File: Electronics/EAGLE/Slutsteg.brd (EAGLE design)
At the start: 100 x 160 mm, 111 parts, among them CN2 OSTYK33102030-2, CN3 OSTYK33102030-2, IC1 MC78M12CDTG, IC10 TM8211, IC11 LM358LVIDR, IC3 TPA3251D2DDVR, IC4 TPA3244DDWR, IC8 ESP32-WROVER-IE-4MB, IC9 ZLDO1117G33TA, J2 0532610671

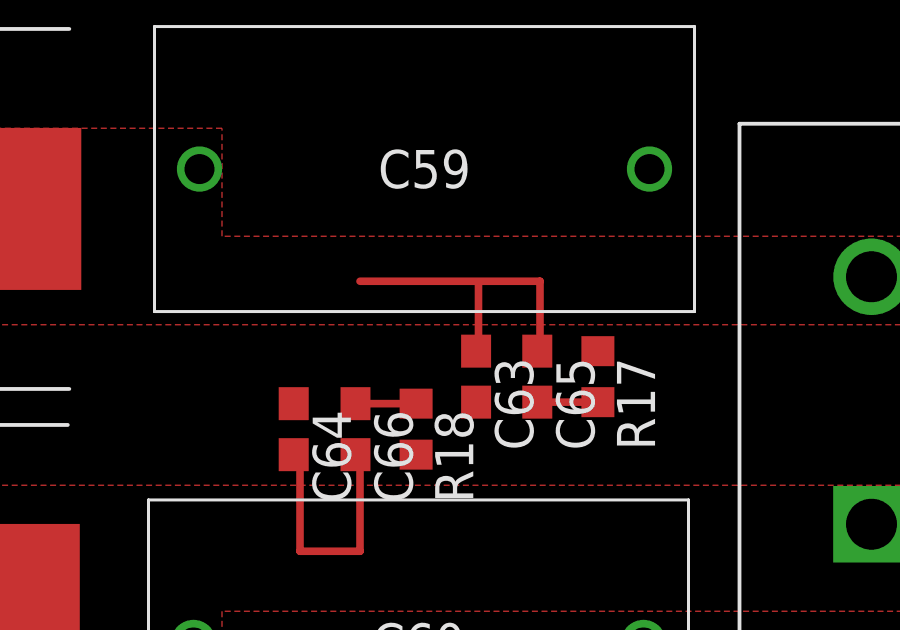
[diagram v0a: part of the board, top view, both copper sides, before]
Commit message: Added speaker connector models.
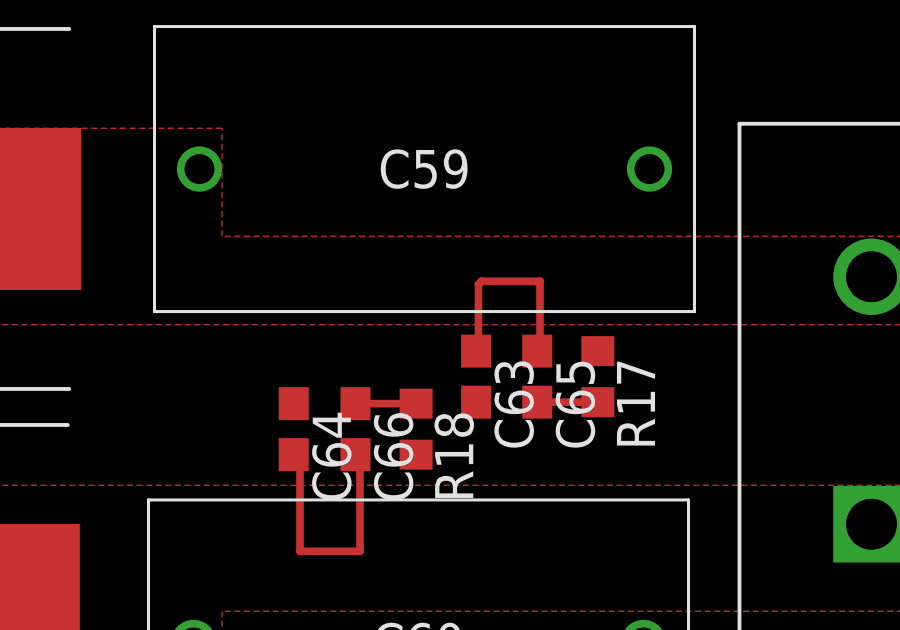
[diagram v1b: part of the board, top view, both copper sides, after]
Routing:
- net SPEAKER_L_0: track 10.6 -> 6.72 mm
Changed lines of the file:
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@@
 <drawing>
 <settings>
-<setting alwaysvectorfont="yes"/>
+<setting alwaysvectorfont="no"/>
 <setting verticaltext="up"/>
 </settings>
@@
 <attribute name="VALUE" x="-35.18" y="73.76" size="1.27" layer="27"/>
 </element>
-<element name="CN2" library="OSTYK33108030" package="OSTYK33108030-2" value="OSTYK33102030-2" x="88.05" y="101.9" smashed="yes" rot="R90">
+<element name="CN2" library="OSTYK33108030" package="OSTYK33108030-2" override_package3d_urn="urn:adsk.eagle:package:27162182/2" override_package_urn="urn:adsk.eagle:footprint:27162183/1" value="OSTYK33102030-2" x="88.05" y="101.9" smashed="yes" rot="R90">
 <attribute name="NAME" x="96.05" y="102.77" size="1.27" layer="25" rot="R90"/>
 </element>
-<element name="CN3" library="OSTYK33108030" package="OSTYK33108030-2" value="OSTYK33102030-2" x="88.05" y="75.8" smashed="yes" rot="R90">
+<element name="CN3" library="OSTYK33108030" package="OSTYK33108030-2" override_package3d_urn="urn:adsk.eagle:package:27162207/2" override_package_urn="urn:adsk.eagle:footprint:27162209/1" value="OSTYK33102030-2" x="88.05" y="75.8" smashed="yes" rot="R90">
 <attribute name="NAME" x="96.05" y="76.67" size="1.27" layer="25" rot="R90"/>
 </element>
@@
 </polygon>
 <wire x1="77" y1="107.76" x2="76.91" y2="107.67" width="0.1524" layer="1"/>
-<wire x1="74.95" y1="109.9" x2="74.95" y2="107.75" width="0.254" layer="1"/>
+<wire x1="74.95" y1="107.75" x2="74.95" y2="109.9" width="0.254" layer="1"/>
 <wire x1="74.87" y1="107.67" x2="74.95" y2="107.75" width="0.254" layer="1"/>
-<wire x1="71" y1="110" x2="77" y2="110" width="0.254" layer="1"/>
 <wire x1="77" y1="110" x2="77" y2="107.76" width="0.254" layer="1"/>
+<wire x1="74.95" y1="109.9" x2="75.05" y2="110" width="0.254" layer="1"/>
+<wire x1="75.05" y1="110" x2="77" y2="110" width="0.254" layer="1"/>
 </signal>
 <signal name="I/O-0">

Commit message: Sammanfogat design blocks
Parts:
- added C12: 150nF/25V, rcl:C0603
- added C13, C14, C55: 1uF/25V, rcl:C0603
- added C56: 33nF/25V, rcl:C0603
- added C87, C88, C89, C90, C91, C92: 100nF/25V, rcl:C0603
- added IC6, IC7: LM324D, SamacSys_Parts:SOIC127P600X175-14N
- added R39, R40, R41, R42, R43, R44: 100K/5%/0.1W, rcl:R0603
- added R45, R46: 1K/5%/0.1W, rcl:R0603
- added R47, R48: 18K/5%/0.1W, rcl:R0603
- added R49, R50, R51, R52, R53, R54, R55: 10K/5%/0.1W, rcl:R0603
- added SW3, SW4: PDB181-K420F-103A2, PDB181-K420F-103A2:SW_420F-103A2_BRN
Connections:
- new net 6V_BUFFER: IC6.1, IC6.2, IC6.5, IC7.12, IC7.3, R51.2, R54.2
- new net BASE_OUT: C56.1, R48.1
- new net BASE_VOLUME: IC6.7
- new net LEFT: C87.1, IC6.13, IC6.14, R45.2
- new net LEFT_OUT: IC7.1, SW3.2, SW3.3
- new net LEFT_VOLUME: IC7.6, IC7.7, R50.1, R52.2
- new net N$46: C13.2, IC6.12, R39.1, R40.2
- new net N$47: C14.2, IC6.10, R41.2, R42.1
- new net N$50: C55.1, IC6.3, R43.1, R44.2
- new net N$66: R45.1, R46.1, R47.2
- new net N$67: C12.2, R47.1, R48.2, R49.2
- new net N$68: C56.2, IC6.6, R49.1
- new net N$69: C87.2, C88.1, R50.2
- new net N$70: C88.2, IC7.5, R51.1
- new net N$71: IC7.2, R52.1, SW3.1
- new net N$72: C90.1, IC7.10, R54.1
- new net N$73: C89.1, C90.2, R53.2
- new net N$74: IC7.13, R55.2, SW4.1
- new net RIGHT: C89.2, IC6.8, IC6.9, R46.2
- new net RIGHT_OUT: IC7.14, SW4.2, SW4.3
- new net RIGHT_VOLUME: IC7.8, IC7.9, R53.1, R55.1
- new net SIG_IN_LEFT: C13.1
- new net SIG_IN_RIGHT: C14.1
- net GND: now also C12.1, C55.2, C91.2, C92.2, IC6.11, IC7.11, R40.1, R41.1, R44.1
- net VDD: now also C91.1, C92.1, IC6.4, IC7.4, R39.2, R42.2, R43.2

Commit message: Minor changes to ESP32 implementation
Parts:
- removed C15, C16, C17, C18, C22: 10uF/50V, rcl:C0805
- removed C19, C20, C21: 100nF/50V, rcl:C0603
- removed C23, C24, C25, C26, C53, C54: 1nF/50V, rcl:C0603
- removed D2: STPS0520Z, SamacSys_Parts:SOD3816X145N
- removed IC10: TM8211, SamacSys_Parts:SOIC127P600X196-8N
- removed IC11: LM358LVIDR, SamacSys_Parts:SOIC127P600X175-8N
- removed IC8: ESP32-WROVER-IE-4MB, SamacSys_Parts:ESP32WROVERE8MB
- removed IC9: ZLDO1117G33TA, SamacSys_Parts:SOT230P700X180-4N
- removed J2: 0532610671, SamacSys_Parts:0532610671
- removed R11, R12, R13, R14, R15: 10k/5%/0.1W, rcl:R0603
- removed SJ2: (no value), jumper:SJ
- added C100, C101, C102: 100nF/50V, rcl:C0603
- added C103, C96, C97, C98, C99: 10uF/50V, rcl:C0805
- added C104, C105, C106, C107, C108, C109: 1nF/50V, rcl:C0603
- added D3: STPS0520Z, SamacSys_Parts:SOD3816X145N
- added IC14: ESP32-WROVER-IE-4MB, SamacSys_Parts:ESP32WROVERE8MB
- added IC15: ZLDO1117G33TA, SamacSys_Parts:SOT230P700X180-4N
- added IC16: TM8211, SamacSys_Parts:SOIC127P600X196-8N
- added IC17: LM358LVIDR, SamacSys_Parts:SOIC127P600X175-8N
- added J3: 0532610671, SamacSys_Parts:0532610671
- added R33, R34, R35, R36, R37, R38, R56, R57, R58, R59, R60: 10k/5%/0.1W, rcl:R0603
- added SJ3: (no value), jumper:SJ
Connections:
- removed net N$15: D2.2, IC9.2, IC9.4, SJ2.1
- removed net N$16: C17.1, C20.1, IC8.2
- removed net N$17: IC10.3, IC8.11
- removed net N$21: IC10.1, IC8.29
- removed net N$22: IC10.2, IC8.10
- removed net N$23: C24.1, IC11.3, R12.1
- removed net N$24: C24.2, C25.1
- removed net N$39: C23.2, R11.1, R12.2
- removed net N$40: C26.1, IC11.5, R13.2
- removed net N$41: C26.2, C53.1
- removed net N$42: C54.2, R13.1, R14.2
- new net N$43: D3.2, IC15.2, IC15.4, SJ3.1
- new net N$75: C101.1, C98.1, IC14.2
- new net N$76: IC14.11, IC16.3
- new net N$77: IC14.29, IC16.1
- new net N$78: IC14.10, IC16.2
- new net N$79: C105.1, IC17.3, R34.1
- new net N$80: C105.2, C106.1
- new net N$81: C107.1, IC17.5, R35.2
- new net N$82: C107.2, C108.1
- new net N$83: C109.2, R35.1, R36.2, R56.1
- new net N$84: C104.2, R33.1, R34.2, R38.1
- new net NEXT: IC14.12, R58.2
- new net PLAY: IC14.8, R60.2
- new net PREV: IC14.16, R57.2
- new net STOP: IC14.9, R59.2
- net +3V3: now also C102.1, C103.1, C96.1, C99.1, D3.1, IC16.5, R37.1, R57.1, R58.1, R59.1, R60.1, SJ3.2; no longer C15.1, C18.1, C21.1, C22.1, D2.1, IC10.5, R15.1, SJ2.2
- net +5V: now also C97.1, IC15.3, J3.1; no longer C16.1, IC9.3, J2.1
- net BLE-L: now also C109.1, IC17.6, IC17.7; no longer C54.1, IC11.6, IC11.7
- net BLE-R: now also C104.1, IC17.1, IC17.2; no longer C23.1, IC11.1, IC11.2
- net DAC-L_N: now also IC16.6, R36.1; no longer IC10.6, R14.1
- net DAC-R_P: now also IC16.8, R33.2; no longer IC10.8, R11.2
- net EN: now also C100.1, IC14.3, J3.4, R37.2; no longer C19.1, IC8.3, J2.4, R15.2
- net GND: now also C100.2, C101.2, C102.2, C103.2, C106.2, C108.2, C96.2, C97.2, C98.2, C99.2, IC14.1, IC14.15, IC14.38, IC14.39, IC14.A39, IC14.B39, IC14.C39, IC14.D39, IC14.E39, IC14.F39, IC14.G39, IC14.H39, IC15.1, IC16.4, IC17.4, J3.6, R38.2, R56.2; no longer C15.2, C16.2, C17.2, C18.2, C19.2, C20.2, C21.2, C22.2, C25.2, C53.2, IC10.4, IC11.4, IC8.1, IC8.15, IC8.38, IC8.39, IC8.A39, IC8.B39, IC8.C39, IC8.D39, IC8.E39, IC8.F39, IC8.G39, IC8.H39, IC9.1, J2.6
- net I/O-0: now also IC14.25, J3.5; no longer IC8.25, J2.5
- net RXD0: now also IC14.34, J3.3; no longer IC8.34, J2.3
- net TXD0: now also IC14.35, J3.2; no longer IC8.35, J2.2
- net VDD: now also IC17.8; no longer IC11.8

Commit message: Renumbered components.
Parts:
- removed C107, C108, C109: 1nF/50V, rcl:C0603
- removed C87, C88, C89, C90, C91, C92: 100nF/25V, rcl:C0603
- removed CN3: OSTYK33102030-2, OSTYK33108030:OSTYK33108030-2
- removed IC14: ESP32-WROVER-IE-4MB, SamacSys_Parts:ESP32WROVERE8MB
- removed IC16: TM8211, SamacSys_Parts:SOIC127P600X196-8N
- removed R48: 18K/5%/0.1W, rcl:R0603
- removed R49, R52, R53, R54, R55: 10K/5%/0.1W, rcl:R0603
- removed R56: 10k/5%/0.1W, rcl:R0603
- added C15, C16, C19, C26, C53, C54: 100nF/50V, rcl:C0603
- added C17: 10nF/50V, rcl:C0603
- added C18: ECA-1HM471B, SamacSys_Parts:CAPPRD500W65D1000H2200
- added C24: 10uF/16V, rcl:C1206
- added CN1: OSTYK33102030-2, OSTYK33108030:OSTYK33108030-2
- added IC8, IC9: LM324D, SamacSys_Parts:SOIC127P600X175-14N
- added R1, R11: 10k/5%/0.1W, rcl:R0603
- added R12, R13, R14, R16: 20K/5%/0.1W, rcl:R0603
- added R15: 3.3R/5%/0.1W, rcl:R0603
- C12: value 150nF/25V -> 1nF/50V
- C13, C14: value 1uF/25V -> 1nF/50V
- C27, C28: value ECA-1HM102B -> 33nF/25V; device TPA3244.dbl:SAMACSYS_PARTS_CAPPRD500W65D1000H2200 -> rcl:C0603
- C29: value B32652A3684J -> 33nF/25V; device SamacSys_Parts:B32652A3684J -> rcl:C0603
- C3, C7, C8: value 10uF/50V -> 10uF/16V
- C30: value B32652A3684J -> ECA-1HM102B; device SamacSys_Parts:B32652A3684J -> SamacSys_Parts:CAPPRD500W65D1000H2200
- C31: value 10nF/50V -> ECA-1HM102B; device rcl:C0603 -> SamacSys_Parts:CAPPRD500W65D1000H2200
- C32: value 10nF/50V -> 33nF/25V
- C33, C34: value 1nF/50V -> PHE426HB7100JR06; device rcl:C0603 -> SamacSys_Parts:PHE426HB7100JR06
- C35, C36: value 33nF/25V -> PHE426HB7100JR06; device rcl:C0603 -> SamacSys_Parts:PHE426HB7100JR06
- C37, C38, C67, C68: value 33nF/25V -> 1nF/50V
- C39: value 100nF/50V -> 1nF/50V
- C40: value 1uF/50V -> 1nF/50V; device rcl:C0805 -> rcl:C0603
- C41, C42, C43, C49: value 1uF/50V -> 10nF/50V; device rcl:C0805 -> rcl:C0603
- C44: value 100nF/50V -> 10nF/50V
- C45: value ECA-1HM471B -> 1uF/50V; device TPA3244.dbl:SAMACSYS_PARTS_CAPPRD500W65D1000H2200 -> rcl:C0805
- C46: value 100nF/50V -> 10uF/16V; device rcl:C0603 -> rcl:C1206
- C47: value 100nF/50V -> ECA-1HM471B; device rcl:C0603 -> TPA3244.dbl:SAMACSYS_PARTS_CAPPRD500W65D1000H2200
- C48: value 10nF/50V -> 1uF/50V; device rcl:C0603 -> rcl:C0805
- C50: value 1uF/50V -> 10uF/16V; device rcl:C0805 -> rcl:C1206
- C51, C52: value 10uF/16V -> 100nF/50V; device rcl:C1206 -> rcl:C0603
- C55: value 1uF/25V -> 33nF/25V
- C56, C57: value 33nF/25V -> 1uF/50V; device rcl:C0603 -> rcl:C0805
- C59, C60: value PHE426HB7100JR06 -> 1uF/50V; device SamacSys_Parts:PHE426HB7100JR06 -> rcl:C0805
- C6: value 100nF/50V -> 10uF/16V
- C61, C62: value PHE426HB7100JR06 -> 33nF/25V; device SamacSys_Parts:PHE426HB7100JR06 -> rcl:C0603
- C63, C64: value 1nF/50V -> ECA-1HM102B; device rcl:C0603 -> TPA3244.dbl:SAMACSYS_PARTS_CAPPRD500W65D1000H2200
- C65, C66: value 10nF/50V -> B32652A3684J; device rcl:C0603 -> SamacSys_Parts:B32652A3684J
- C69, C70: value 1nF/50V -> 10nF/50V
- C71, C72: value 10nF/50V -> 100nF/25V
- C73: value ECA-1HM102B -> 150nF/25V; device SamacSys_Parts:CAPPRD500W65D1000H2200 -> rcl:C0603
- C74: value ECA-1HM102B -> 100nF/25V; device SamacSys_Parts:CAPPRD500W65D1000H2200 -> rcl:C0603
- C75: value 100nF/50V -> 33nF/25V
- C76: value 10nF/50V -> 1uF/25V
- C77, C80: value 100nF/50V -> 100nF/25V
- C78: value 100nF/50V -> 1uF/25V
- C79: value ECA-1HM471B -> 1uF/25V; device SamacSys_Parts:CAPPRD500W65D1000H2200 -> rcl:C0603
- C81: value 10uF/16V -> 100nF/25V; device rcl:C1206 -> rcl:C0603
- IC3: value TPA3251D2DDVR -> ESP32-WROVER-IE-4MB; device SamacSys_Parts:SOP64P810X120-45N@1 -> SamacSys_Parts:ESP32WROVERE8MB
- IC4: value TPA3244DDWR -> TM8211; device SamacSys_Parts:SOP64P810X120-45N -> SamacSys_Parts:SOIC127P600X196-8N
- IC6: value LM324D -> TPA3244DDWR; device SamacSys_Parts:SOIC127P600X175-14N -> SamacSys_Parts:SOP64P810X120-45N
- IC7: value LM324D -> TPA3251D2DDVR; device SamacSys_Parts:SOIC127P600X175-14N -> SamacSys_Parts:SOP64P810X120-45N@1
- R10, R6, R7, R9: value 3.3R/5%/0.1W -> 10k/5%/0.1W
- R17: value 3.3R/5%/0.1W -> 20K/5%/0.1W
- R21, R24, R26, R27: value 20K/5%/0.1W -> 3.3R/5%/0.1W
- R33: value 10k/5%/0.1W -> 18K/5%/0.1W
- R34, R35, R38: value 10k/5%/0.1W -> 10K/5%/0.1W
- R36, R37: value 10k/5%/0.1W -> 100K/5%/0.1W
- R41, R44: value 100K/5%/0.1W -> 10K/5%/0.1W
- R8: value 20K/5%/0.1W -> 10k/5%/0.1W
- moved R7 413.4 mm to (-206.8, 80.5)
- moved R6 380.7 mm to (-206.8, 136.4)
- moved R8 370.2 mm to (-206.8, 131.3)
- moved R10 329.5 mm to (-206.8, 75.5)
- moved R9 325.9 mm to (-206.8, 100.9)
- moved IC7 303.8 mm to (139.4, 197.2)
- moved C56 294.9 mm to (116.5, 91.8)
- moved C55 293.8 mm to (115.3, 114.6)
- moved C73 270.3 mm to (-138.8, 288.1), turned to 0 degrees
- moved C72 268.7 mm to (-165.5, 195.4), turned to 0 degrees
- moved C71 264.2 mm to (-165.5, 199.2), turned to 0 degrees
- moved IC6 252.1 mm to (32.2, 92.9)
- moved IC4 250.0 mm to (-196.7, 193.6)
- moved C79 234.7 mm to (-156.6, 237.3), turned to 0 degrees
- moved C57 223.7 mm to (116.5, 85.4)
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- renumbered C100 to C1, C101 to C2, C102 to C6, C103 to C8, C104 to C9, C105 to C10, C106 to C11, C82 to C21, C83 to C25, C84 to C22, C85 to C20, C86 to C23, C96 to C5, C97 to C4, C98 to C3, C99 to C7, D3 to D1, IC15 to IC2, IC17 to IC5, J3 to J1, L10 to L2, L11 to L3, L12 to L4, L9 to L1, R45 to R28, R46 to R29, R47 to R31, R50 to R30, R51 to R32, R57 to R2, R58 to R3, R59 to R4, R60 to R5, SJ3 to SJ1, SW3 to SW1, SW4 to SW2
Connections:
- net +3V3: now also IC4.5, R1.1, R12.2, R13.2, R14.2; no longer IC16.5, R25.2, R26.2, R27.2, R37.1
- net 6V_BUFFER: now also IC8.12, IC8.3, IC9.1, IC9.2, IC9.5, R41.2; no longer IC6.1, IC6.2, IC6.5, IC7.12, IC7.3, R54.2
- net BASE_OUT: now also C75.1, R33.1; no longer C56.1, R48.1
- net BASE_VOLUME: now also IC9.7; no longer IC6.7
- net BLE-L: now also C14.1; no longer C109.1
- net CLIP_OTW: now also IC6.2, IC7.21, R14.1; no longer IC3.21, IC4.2, R25.1
- net DAC-L_N: now also IC4.6, R11.1; no longer IC16.6, R36.1
- net DAC-R_P: now also IC4.8, R6.2; no longer IC16.8, R33.2
- net EN: now also IC3.3, R1.2; no longer IC14.3, R37.2
- net FAULT: now also IC6.4, IC7.19, R13.1; no longer IC3.19, IC4.4, R26.1
- net GND: now also C13.2, C15.2, C16.2, C17.2, C18.2, C19.2, C26.2, C30.2, C31.2, C35.1, C36.2, C37.2, C38.1, C40.1, C45.1, C47.2, C51.1, C52.2, C53.2, C54.2, C56.2, C57.1, C64.2, C65.1, C66.2, C67.2, C68.1, C73.1, IC3.1, IC3.15, IC3.38, IC3.39, IC3.A39, IC3.B39, IC3.C39, IC3.D39, IC3.E39, IC3.F39, IC3.G39, IC3.H39, IC4.4, IC6.10, IC6.19, IC6.20, IC6.25, IC6.26, IC6.33, IC6.34, IC6.41, IC6.42, IC6.45, IC7.12, IC7.13, IC7.16, IC7.17, IC7.25, IC7.26, IC7.3, IC7.33, IC7.34, IC7.41, IC7.42, IC7.45, IC8.11, IC9.11, R10.2, R16.1, R22.2, R25.1, R26.1, R27.2, R37.1, R43.1, R7.2; no longer C108.2, C12.1, C27.2, C28.2, C29.2, C30.1, C40.2, C41.2, C42.1, C43.1, C44.2, C45.2, C46.2, C47.1, C50.1, C55.2, C61.1, C62.2, C64.1, C69.2, C70.1, C73.2, C75.2, C78.2, C79.2, C80.2, C91.2, C92.2, IC14.1, IC14.15, IC14.38, IC14.39, IC14.A39, IC14.B39, IC14.C39, IC14.D39, IC14.E39, IC14.F39, IC14.G39, IC14.H39, IC16.4, IC3.12, IC3.13, IC3.16, IC3.17, IC3.25, IC3.26, IC3.3, IC3.33, IC3.34, IC3.41, IC3.42, IC3.45, IC4.10, IC4.11, IC4.19, IC4.20, IC4.25, IC4.26, IC4.33, IC4.34, IC4.41, IC4.42, IC4.45, IC7.11, R10.1, R18.2, R24.1, R38.2, R41.1, R44.1, R56.2, R8.1, R9.2
- net I/O-0: now also IC3.25; no longer IC14.25
- net INPUT_A_SLAVE: now also C46.2; no longer C52.2
- net INPUT_B_SLAVE: now also C50.2; no longer C51.2
- net INPUT_D: now also C24.2; no longer C81.2
- net LEFT: now also C71.1, IC9.13, IC9.14; no longer C87.1, IC6.13, IC6.14
- net LEFT_OUT: now also IC8.1; no longer IC7.1
- net LEFT_VOLUME: now also IC8.6, IC8.7, R35.2; no longer IC7.6, IC7.7, R52.2
- net N$1: now also IC6.12; no longer IC4.12
- net N$18: now also C55.2, IC7.39, IC7.40; no longer C37.2, IC3.39, IC3.40
- net N$19: now also C61.2, IC7.35; no longer C38.2, IC3.35
- net N$2: now also C70.1, R27.1; no longer C31.1, R9.1
- net N$20: now also C58.1, IC7.23; no longer C36.1, IC3.23
- net N$25: now also C62.1, IC7.24; no longer C35.1, IC3.24
- net N$26: now also C62.2, IC7.32, L7.1; no longer C35.2, IC3.32, L8.1
- net N$27: now also C46.1, IC7.5; no longer C52.1, IC3.5
- net N$28: now also C50.1, IC7.6; no longer C51.1, IC3.6
- net N$29: now also C53.1, IC7.1, R23.2; no longer C46.1, IC3.1, R6.2
- net N$3: now also C55.1, IC7.44; no longer C37.1, IC3.44
- net N$30: now also C51.2, IC7.20; no longer C47.2, IC3.20
- net N$31: now also C49.2, IC7.15; no longer C48.2, IC3.15
- net N$32: now also C45.2, IC7.14; no longer C49.2, IC3.14
- net N$33: now also C48.2, IC7.11, IC7.4, IC7.8; no longer C50.2, IC3.11, IC3.4, IC3.8
- net N$34: now also IC7.7, R25.2; no longer IC3.7, R8.2
- net N$35: now also C61.1, IC7.43; no longer C38.1, IC3.43
- net N$36: now also C58.2, IC7.27, IC7.28, L8.1; no longer C36.2, IC3.27, IC3.28, L7.1
- net N$37: now also C54.1, IC7.22, R24.2; no longer C39.1, IC3.22, R7.2
- net N$38: now also C69.2, R26.2; no longer C32.2, R10.2
- net N$44: now also C27.1, IC6.44; no longer C57.1, IC4.44
- net N$45: now also C29.1, IC6.43; no longer C58.1, IC4.43
- net N$46: now also C78.2, IC9.12; no longer C13.2, IC6.12
- net N$47: now also C79.2, IC9.10, R43.2; no longer C14.2, IC6.10, R41.2
- net N$48: now also C41.2, R19.2; no longer C65.2, R17.2
- net N$49: now also C42.1, R20.1; no longer C66.1, R18.1
- net N$50: now also C76.1, IC9.3, R36.1, R37.2; no longer C55.1, IC6.3, R43.1, R44.2
- net N$51: now also C28.1, IC6.24; no longer C68.1, IC4.24
- net N$52: now also C32.1, IC6.23; no longer C67.1, IC4.23
- net N$53: now also C43.2, R21.2; no longer C71.2, R19.2
- net N$54: now also C44.1, R22.1; no longer C72.1, R20.1
- net N$55: now also IC6.15, R17.2; no longer IC4.15, R21.2
- net N$56: now also C16.1, IC6.3; no longer C75.1, IC4.3
- net N$57: now also C17.1, IC6.8; no longer C76.1, IC4.8
- net N$58: now also IC6.9; no longer IC4.9
- net N$59: now also C15.1, IC6.1, R15.1; no longer C77.1, IC4.1, R22.1
- net N$60: now also C26.1, IC6.22, R18.1; no longer C78.1, IC4.22, R23.1
- net N$61: now also C24.1, IC6.6; no longer C81.1, IC4.6
- net N$62: now also IC6.7; no longer IC4.7
- net N$63: now also IC6.17; no longer IC4.17
- net N$64: now also IC6.18; no longer IC4.18
- net N$65: now also IC6.16, R16.2; no longer IC4.16, R24.2
- net N$67: now also C73.2, R33.2, R34.2; no longer C12.2, R48.2, R49.2
- net N$68: now also C75.2, IC9.6, R34.1; no longer C56.2, IC6.6, R49.1
- net N$69: now also C71.2, C72.1; no longer C87.2, C88.1
- net N$70: now also C72.2, IC8.5; no longer C88.2, IC7.5
- net N$71: now also IC8.2, R35.1; no longer IC7.2, R52.1
- net N$72: now also C80.1, IC8.10, R41.1; no longer C90.1, IC7.10, R54.1
- net N$73: now also C80.2, C81.1, R44.2; no longer C89.1, C90.2, R53.2
- net N$74: now also IC8.13, R38.2; no longer IC7.13, R55.2
- net N$75: now also IC3.2; no longer IC14.2
- net N$76: now also IC3.11, IC4.3; no longer IC14.11, IC16.3
- net N$77: now also IC3.29, IC4.1; no longer IC14.29, IC16.1
- net N$78: now also IC3.10, IC4.2; no longer IC14.10, IC16.2
- net N$79: now also R8.1; no longer R34.1
- net N$81: now also C12.1, R9.2; no longer C107.1, R35.2
- net N$82: now also C12.2, C13.1; no longer C107.2, C108.1
- net N$83: now also C14.2, R10.1, R11.2, R9.1; no longer C109.2, R35.1, R36.2, R56.1
- net N$84: now also R6.1, R7.1, R8.2; no longer R33.1, R34.2, R38.1
- net NEXT: now also IC3.12; no longer IC14.12
- net OSC_IOM: now also IC6.14, IC7.10; no longer IC3.10, IC4.14
- net OSC_IOP: now also IC6.13, IC7.9; no longer IC3.9, IC4.13
- net OUT_A: now also C32.2, IC6.27, IC6.28; no longer C67.2, IC4.27, IC4.28
- net OUT_B: now also C28.2, IC6.32; no longer C68.2, IC4.32
- net OUT_C: now also C29.2, IC6.35; no longer C58.2, IC4.35
- net OUT_D: now also C27.2, IC6.39, IC6.40; no longer C57.2, IC4.39, IC4.40
- net PLAY: now also IC3.8; no longer IC14.8
- net PREV: now also IC3.16; no longer IC14.16
- net PVDD: now also C30.1, C31.1, C56.1, C57.2, C59.2, C60.1, C63.1, C64.1, IC6.29, IC6.30, IC6.31, IC6.36, IC6.37, IC6.38, IC7.29, IC7.30, IC7.31, IC7.36, IC7.37, IC7.38; no longer C27.1, C28.1, C40.1, C41.1, C42.2, C43.2, C73.1, C74.1, IC3.29, IC3.30, IC3.31, IC3.36, IC3.37, IC3.38, IC4.29, IC4.30, IC4.31, IC4.36, IC4.37, IC4.38
- net RESET: now also IC6.5, IC7.18, R12.1; no longer IC3.18, IC4.5, R27.1
- net RIGHT: now also C81.2, IC9.8, IC9.9; no longer C89.2, IC6.8, IC6.9
- net RIGHT_OUT: now also IC8.14; no longer IC7.14
- net RIGHT_VOLUME: now also IC8.8, IC8.9, R38.1, R44.1; no longer IC7.8, IC7.9, R53.1, R55.1
- net RXD0: now also IC3.34; no longer IC14.34
- net SIG_IN_LEFT: now also C78.1; no longer C13.1
- net SIG_IN_RIGHT: now also C79.1; no longer C14.1
- net SPEAKER_B_0: now also C65.2, C67.1, C69.1, L7.2; no longer C30.2, C32.1, C34.1, L8.2
- net SPEAKER_B_1: now also C66.1, C68.2, C70.2, L8.2; no longer C29.1, C31.2, C33.2, L7.2
- net SPEAKER_L_0: now also C33.2, C37.1, C41.1, CN1.2; no longer C59.2, C63.1, C65.1, CN2.2
- net SPEAKER_L_1: now also C34.1, C38.2, C42.2, CN1.1; no longer C60.1, C64.2, C66.2, CN2.1
- net SPEAKER_R_0: now also C35.2, C39.1, C43.1, CN2.2; no longer C61.2, C69.1, C71.1, CN3.2
- net SPEAKER_R_1: now also C36.1, C40.2, C44.2, CN2.1; no longer C62.1, C70.2, C72.2, CN3.1
- net STOP: now also IC3.9; no longer IC14.9
- net TXD0: now also IC3.35; no longer IC14.35
- net VDD: now also C18.1, C19.1, C47.1, C52.1, C74.1, C77.1, IC6.21, IC7.2, IC8.4, IC9.4, R15.2, R18.2, R23.1, R24.1, R36.2; no longer C44.1, C45.1, C79.1, C80.1, C91.1, C92.1, IC3.2, IC4.21, IC6.4, IC7.4, R22.2, R23.2, R43.2, R6.1, R7.1

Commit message: Updated components value
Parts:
- added CN3, CN4: OSTYK33102030-2, OSTYK33108030:OSTYK33108030-2
- added IC10: LM324D, SamacSys_Parts:SOIC127P600X175-14N
- C4, C5: value 10uF/50V -> 10uF/16V
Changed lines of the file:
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@@
 <attribute name="VALUE" x="-199.21" y="217.71" size="1.27" layer="27" align="center"/>
 </element>
-<element name="C5" library="rcl" library_urn="urn:adsk.eagle:library:334" package="C0805" package3d_urn="urn:adsk.eagle:package:23617/2" value="10uF/50V" x="-204.29" y="210.09" smashed="yes">
+<element name="C5" library="rcl" library_urn="urn:adsk.eagle:library:334" package="C0805" package3d_urn="urn:adsk.eagle:package:23617/2" value="10uF/16V" x="-204.29" y="210.09" smashed="yes">
 <attribute name="NAME" x="-205.56" y="211.36" size="1.27" layer="25"/>
 <attribute name="POPULARITY" value="88" x="-204.29" y="210.09" size="1.778" layer="27" display="off"/>
@@
 <attribute name="VALUE" x="-205.56" y="207.55" size="1.27" layer="27"/>
 </element>
-<element name="C4" library="rcl" library_urn="urn:adsk.eagle:library:334" package="C0805" package3d_urn="urn:adsk.eagle:package:23617/2" value="10uF/50V" x="-204.29" y="205.01" smashed="yes">
+<element name="C4" library="rcl" library_urn="urn:adsk.eagle:library:334" package="C0805" package3d_urn="urn:adsk.eagle:package:23617/2" value="10uF/16V" x="-204.29" y="205.01" smashed="yes">
 <attribute name="NAME" x="-205.56" y="206.28" size="1.27" layer="25"/>
 <attribute name="POPULARITY" value="88" x="-204.29" y="205.01" size="1.778" layer="27" display="off"/>
@@
 <attribute name="VALUE" x="-207.465" y="53.245" size="1.27" layer="27"/>
 </element>
+<element name="IC10" library="SamacSys_Parts" package="SOIC127P600X175-14N" value="LM324D" x="-204" y="-6" smashed="yes">
+<attribute name="ARROW_PART_NUMBER" value="LM324D" x="-213" y="4" size="1.778" layer="27" display="off"/>
+<attribute name="ARROW_PRICE-STOCK" value="https://www.arrow.com/en/products/lm324d/stmicroelectronics" x="-213" y="4" size="1.778" layer="27" display="off"/>
+<attribute name="DESCRIPTION" value="LM324D, Quad Operational Amplifier 1.3MHz 5 to 28V, 14-Pin SO" x="-213" y="4" size="1.778" layer="27" display="off"/>
+<attribute name="HEIGHT" value="1.75mm" x="-213" y="4" size="1.778" layer="27" display="off"/>
+<attribute name="MANUFACTURER_NAME" value="STMicroelectronics" x="-213" y="4" size="1.778" layer="27" display="off"/>
+<attribute name="MANUFACTURER_PART_NUMBER" value="LM324D" x="-213" y="4" size="1.778" layer="27" display="off"/>
+<attribute name="MOUSER_PART_NUMBER" value="511-LM324D" x="-213" y="4" size="1.778" layer="27" display="off"/>
+<attribute name="MOUSER_PRICE-STOCK" value="https://www.mouser.co.uk/ProductDetail/STMicroelectronics/LM324D/?qs=eb%2FRSZx1fMu8HpwSZod0Vw%3D%3D" x="-213" y="4" size="1.778" layer="27" display="off"/>
+<attribute name="NAME" x="-204" y="-6" size="1.27" layer="25" align="center"/>
+<attribute name="VALUE" x="-204" y="-6" size="1.27" layer="27" align="center"/>
+</element>
+<element name="CN3" library="OSTYK33108030" package="OSTYK33108030-2" override_package3d_urn="urn:adsk.eagle:package:27162182/2" override_package_urn="urn:adsk.eagle:footprint:27162183/1" value="OSTYK33102030-2" x="95" y="44" smashed="yes" rot="R270">
+<attribute name="NAME" x="87" y="43.13" size="1.27" layer="25" rot="R270"/>
+</element>
+<element name="CN4" library="OSTYK33108030" package="OSTYK33108030-2" override_package3d_urn="urn:adsk.eagle:package:27162207/2" override_package_urn="urn:adsk.eagle:footprint:27162209/1" value="OSTYK33102030-2" x="95" y="14" smashed="yes" rot="R270">
+<attribute name="NAME" x="87" y="13.13" size="1.27" layer="25" rot="R270"/>
+</element>
 </elements>

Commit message: Changed some component footprints and simplified the V-Reg configuration
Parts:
- removed C25: 10uF/16V, rcl:C1206
- removed IC2: ZLDO1117G33TA, SamacSys_Parts:SOT230P700X180-4N
- removed SJ1: (no value), jumper:SJ
- added C82: 10uF/16V, rcl:C0805
- added IC11: L78M12ABDT-TR, SamacSys_Parts:TO228P972X240-3N
- C21, C22, C24: device rcl:C1206 -> rcl:C0805
- C6: device rcl:C0603 -> rcl:C0805
- IC1: value MC78M12CDTG -> SPX1117M3-L-3-3_TR; device linear:DPACK_3 -> SamacSys_Parts:SOT230P700X180-4N
- moved C24 314.4 mm to (-212.0, -65.0)
- moved C22 305.1 mm to (-212.0, -72.0)
- moved C21 304.1 mm to (-212.0, -58.0)
- moved C5 247.2 mm to (-212.0, -37.0)
- moved IC1 246.5 mm to (-205.0, -23.0)
- moved C4 235.1 mm to (-212.0, -30.0)
- moved C6 211.7 mm to (-212.0, -51.0)
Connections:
- removed net N$43: D1.2, IC2.2, IC2.4, SJ1.1
- net +3V3: now also IC1.2, IC1.4; no longer D1.1, SJ1.2
- net +5V: now also D1.2; no longer C4.1, IC2.3
- net CLIP_OTW: now also IC3.33
- net FAULT: now also IC3.36
- net GND: now also IC1.1, IC11.4; no longer IC1.4, IC2.1
- net INPUT_A: now also C22.1; no longer C22.2
- net INPUT_B: now also C24.1; no longer C25.2
- net INPUT_C: now also C21.1; no longer C21.2
- net INPUT_D: now also C82.1; no longer C24.2
- net N$61: now also C82.2; no longer C24.1
- net N$62: now also C21.2; no longer C21.1
- net N$63: now also C24.2; no longer C25.1
- net N$64: now also C22.2; no longer C22.1
- net PVDD: now also IC11.1
- net RESET: now also IC3.37
- net VDD: now also C4.1, D1.1, IC1.3, IC11.3
